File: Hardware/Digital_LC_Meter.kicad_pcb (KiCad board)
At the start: 2 copper layers, 139.7 x 139.7 mm, 0 parts

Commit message: updated kicad files
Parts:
- added C_BP1: 100nF, Capacitor_THT:C_Rect_L7.0mm_W2.0mm_P5.00mm, F.Cu at (127.0, 137.2)
- added C_COUP1: 10uF, Capacitor_THT:CP_Radial_D5.0mm_P2.50mm, F.Cu at (147.3, 120.7)
- added C_MICA1: 1nF, Capacitor_THT:C_Rect_L7.0mm_W2.0mm_P5.00mm, F.Cu at (152.4, 163.8)
- added C_MICA2: 1nF, Capacitor_THT:C_Rect_L7.0mm_W2.0mm_P5.00mm, F.Cu at (163.8, 158.8)
- added C_OSC1: 10uF, Capacitor_THT:CP_Radial_D5.0mm_P2.50mm, F.Cu at (102.9, 116.8)
- added J_CALJUMPER1: Conn_01x02, Connector_PinHeader_2.54mm:PinHeader_1x02_P2.54mm_Vertical, F.Cu at (83.8, 161.3)
- added J_DA1: Conn_01x01, Connector_PinHeader_2.54mm:PinHeader_1x01_P2.54mm_Vertical, F.Cu at (158.8, 83.8)
- added J_DK1: Conn_01x01, Connector_PinHeader_2.54mm:PinHeader_1x01_P2.54mm_Vertical, F.Cu at (166.4, 83.8)
- added J_ERASEBTN1: Conn_01x02, Connector_PinHeader_2.54mm:PinHeader_1x02_P2.54mm_Vertical, F.Cu at (73.7, 161.3)
- added J_INPUT1: Conn_01x02, Connector_PinHeader_2.54mm:PinHeader_1x02_P2.54mm_Vertical, F.Cu at (129.5, 97.8)
- added J_LCSELECTSPDT1: Conn_01x06, Connector_PinHeader_2.54mm:PinHeader_1x06_P2.54mm_Vertical, F.Cu at (138.4, 102.9)
- added J_NANOTX1: Conn_01x15, Connector_PinHeader_2.54mm:PinHeader_1x15_P2.54mm_Vertical, F.Cu at (52.1, 92.7)
- added J_NANOVIN1: Conn_01x15, Connector_PinHeader_2.54mm:PinHeader_1x15_P2.54mm_Vertical, F.Cu at (67.3, 92.7)
- added J_NUDGEBTN1: Conn_01x03, Connector_PinHeader_2.54mm:PinHeader_1x03_P2.54mm_Vertical, F.Cu at (92.7, 161.3)
- added J_OLED1: Conn_01x04, Connector_PinHeader_2.54mm:PinHeader_1x04_P2.54mm_Vertical, F.Cu at (118.1, 161.3)
- added J_PWR1: Conn_01x02, Connector_PinHeader_2.54mm:PinHeader_1x02_P2.54mm_Vertical, F.Cu at (153.7, 142.2)
- added J_RESETBTN1: Conn_01x02, Connector_PinHeader_2.54mm:PinHeader_1x02_P2.54mm_Vertical, F.Cu at (130.8, 161.3)
- added L1: 100uH, Inductor_THT:L_Radial_D7.8mm_P5.00mm_Fastron_07HCP, F.Cu at (147.3, 96.5)
- added R3: 100K, Resistor_THT:R_Axial_DIN0207_L6.3mm_D2.5mm_P7.62mm_Horizontal, F.Cu at (128.3, 115.6)
- added R_BIAS1: 100K, Resistor_THT:R_Axial_DIN0207_L6.3mm_D2.5mm_P7.62mm_Horizontal, F.Cu at (135.9, 113.0)
- added R_BIAS2: 100K, Resistor_THT:R_Axial_DIN0207_L6.3mm_D2.5mm_P7.62mm_Horizontal, F.Cu at (105.4, 108.0)
- added R_BIAS3: 4K7, Resistor_THT:R_Axial_DIN0207_L6.3mm_D2.5mm_P7.62mm_Horizontal, F.Cu at (119.4, 97.8)
- added R_OSC1: 47K, Resistor_THT:R_Axial_DIN0207_L6.3mm_D2.5mm_P7.62mm_Horizontal, F.Cu at (119.4, 127.0)
- added R_SIG1: 6K8, Resistor_THT:R_Axial_DIN0207_L6.3mm_D2.5mm_P7.62mm_Horizontal, F.Cu at (111.8, 91.4)
- added U_OSC1: LM311, Package_DIP:DIP-8_W7.62mm_Socket, F.Cu at (111.8, 113.0)
- added U_RLY1: TE_ReedRelay_V23100V4xxxA010, TE_Reed_Relay_V23100V4:TE_ReedRelay_V23100V4, F.Cu at (163.8, 101.6)
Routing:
- net /GND: track 0.00 -> 511.2 mm
- net /5V: track 0.00 -> 205.8 mm
- net /RELAY_PIN3: track 0.00 -> 171.1 mm
- net /VIN: track 0.00 -> 123.2 mm
- net /DECR_PIN4: track 0.00 -> 120.9 mm
- net /CL_BAR_PIN2: track 0.00 -> 117.9 mm
- net /IND_PARALLEL: track 0.11 -> 110.6 mm
- net /RESET_PIN: track 0.00 -> 107.0 mm
- net /OSC_SIG_PIN5: track 0.00 -> 100.7 mm
- net /SDA: track 0.00 -> 82.3 mm
- net /SCL: track 0.00 -> 81.5 mm
- net Net-(C_COUP1-Pad1): track 0.00 -> 75.5 mm
- net /CAL_ERASE_PIN8: track 0.00 -> 75.1 mm
- net /INCR_PIN6: track 0.00 -> 68.8 mm
- net /CAL_LK_PIN7: track 0.00 -> 60.4 mm
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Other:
- board size 139.7 x 139.7 mm -> 139.7 x 109.2 mm

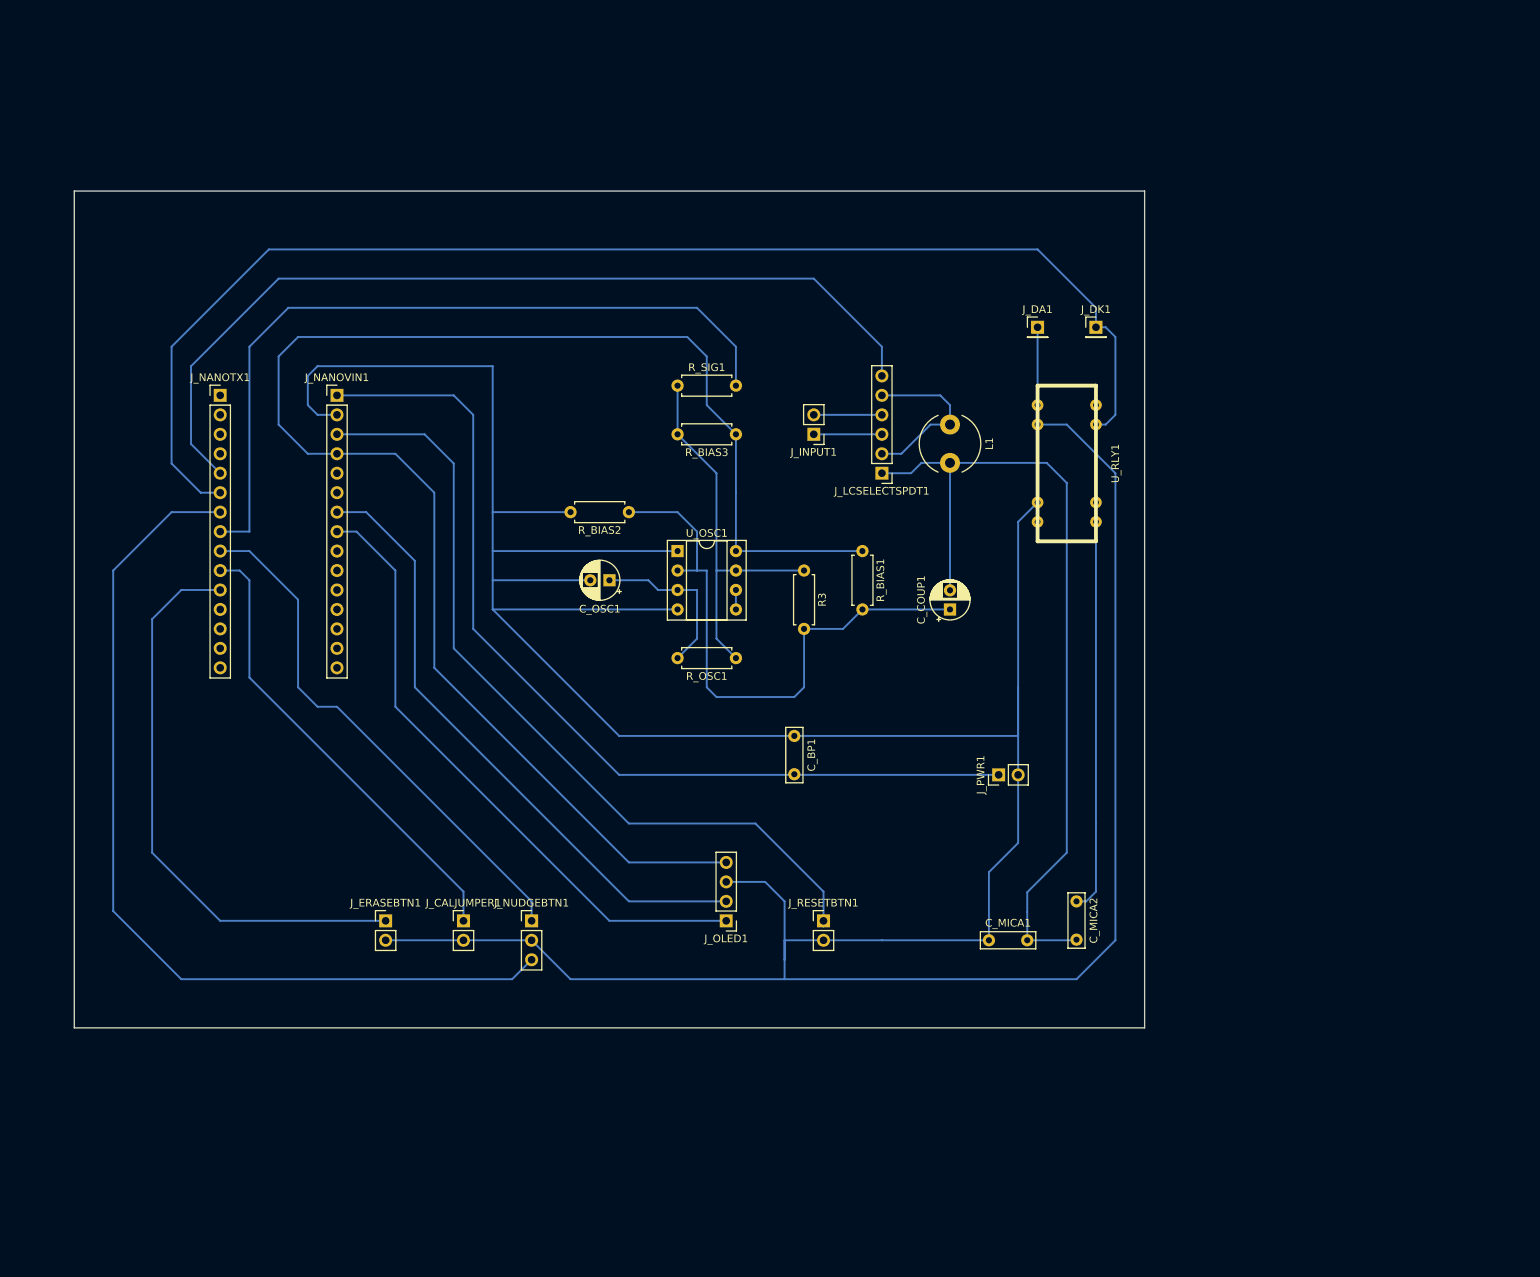
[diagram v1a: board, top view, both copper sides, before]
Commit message: Added 2nd OLED and TCA9548A IICMux. Updated Schematic and Board Layouts
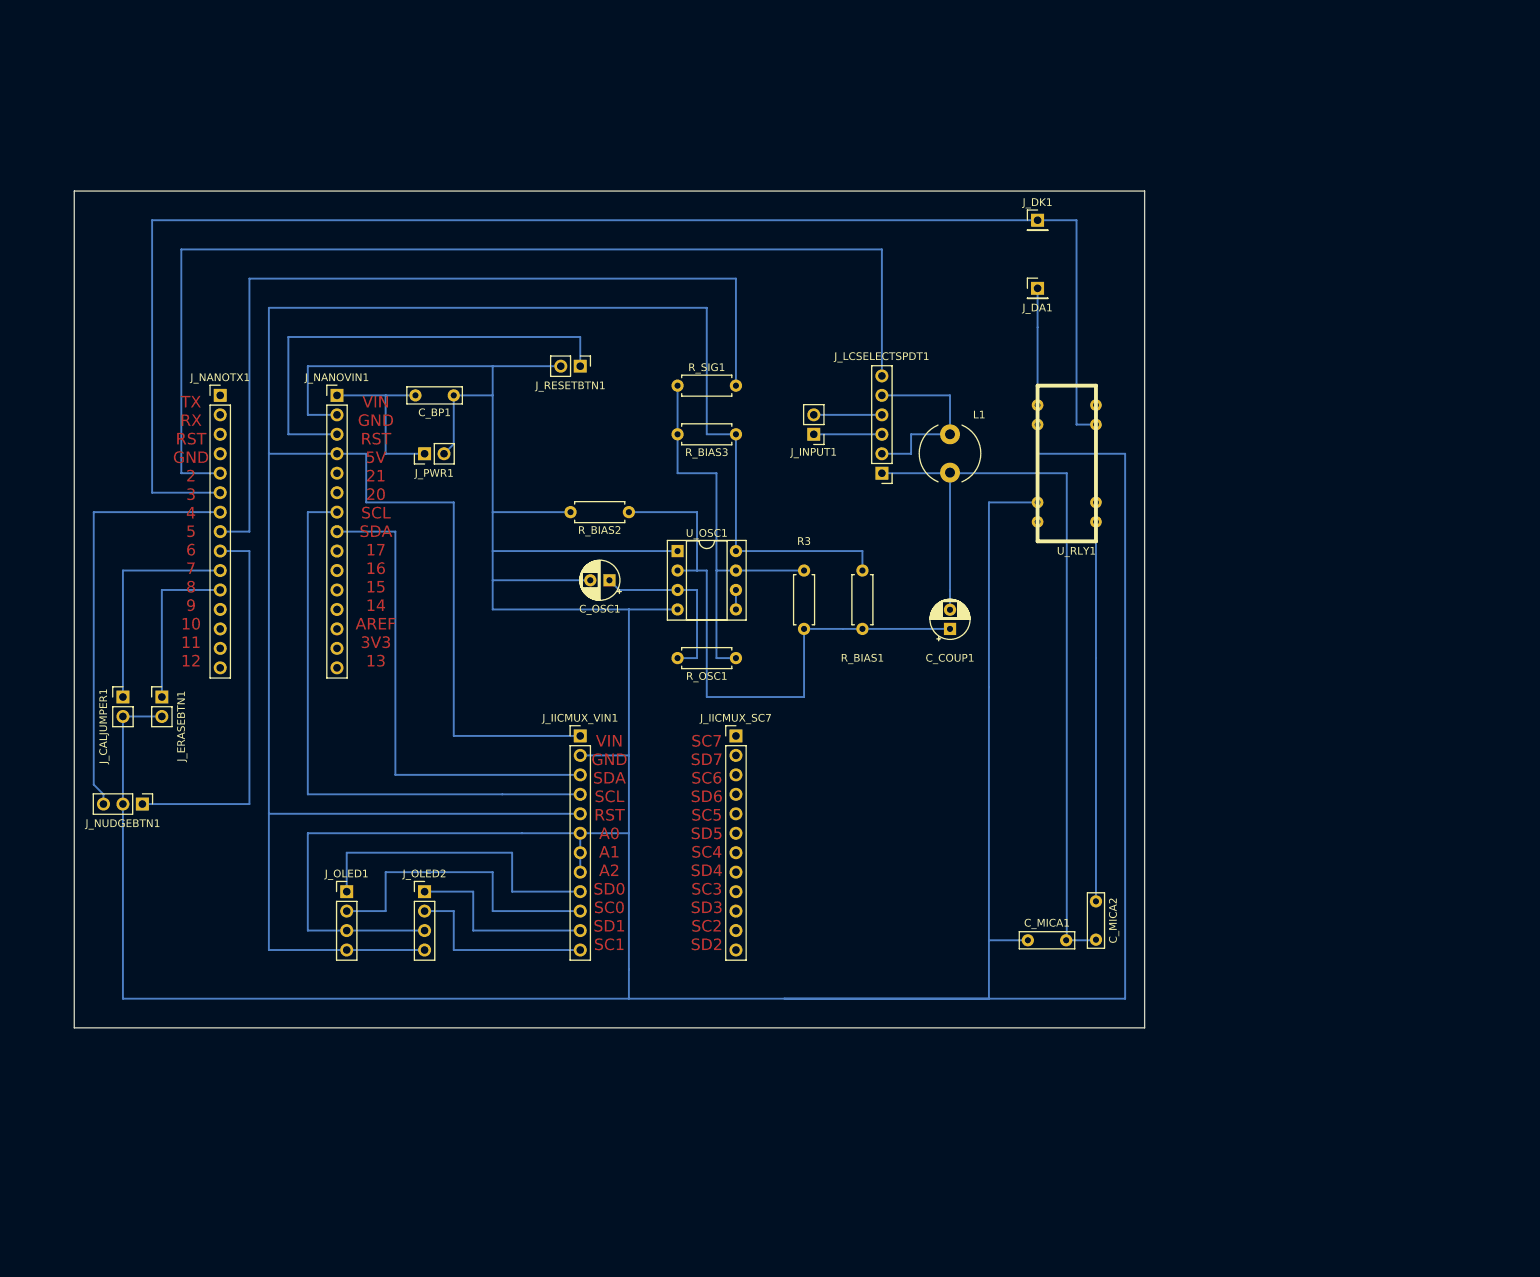
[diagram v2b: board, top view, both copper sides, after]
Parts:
- added J_IICMUX_SC7: Conn_01x12, Connector_PinHeader_2.54mm:PinHeader_1x12_P2.54mm_Vertical, F.Cu at (119.4, 137.2)
- added J_IICMUX_VIN1: Conn_01x12, Connector_PinHeader_2.54mm:PinHeader_1x12_P2.54mm_Vertical, F.Cu at (99.1, 137.2)
- added J_OLED2: Conn_01x04, Connector_PinHeader_2.54mm:PinHeader_1x04_P2.54mm_Vertical, F.Cu at (78.7, 157.5)
- moved J_PWR1 85.9 mm to (78.7, 100.3)
- moved J_RESETBTN1 79.0 mm to (99.1, 88.9), turned to 270 degrees
- moved C_BP1 62.9 mm to (82.5, 92.7), turned to 180 degrees
- moved J_CALJUMPER1 53.2 mm to (39.4, 132.1)
- moved J_NUDGEBTN1 53.0 mm to (41.9, 146.1), turned to 270 degrees
- moved J_OLED1 49.7 mm to (68.6, 157.5), turned to 0 degrees
- moved J_ERASEBTN1 41.3 mm to (44.5, 132.1)
- moved J_DK1 15.9 mm to (158.8, 69.8)
- moved J_DA1 5.08 mm to (158.8, 78.7)
- moved C_MICA1 5.08 mm to (157.5, 163.8)
- moved C_COUP1 2.54 mm to (147.3, 123.2)
- moved C_MICA2 2.54 mm to (166.4, 158.8)
- moved R_BIAS1 2.54 mm to (135.9, 115.6)
- moved L1 1.27 mm to (147.3, 97.8)
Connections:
- J_NANOTX1 pad 1: Net-(J_NANOTX1-Pad1) -> (no net)
- J_NANOTX1 pad 12: Net-(J_NANOTX1-Pad12) -> (no net)
- J_NANOTX1 pad 13: Net-(J_NANOTX1-Pad13) -> (no net)
- J_NANOTX1 pad 14: Net-(J_NANOTX1-Pad14) -> (no net)
- J_NANOTX1 pad 15: Net-(J_NANOTX1-Pad15) -> (no net)
- J_NANOTX1 pad 2: Net-(J_NANOTX1-Pad2) -> (no net)
- J_NANOTX1 pad 3: Net-(J_NANOTX1-Pad3) -> (no net)
- J_NANOTX1 pad 4: Net-(J_NANOTX1-Pad4) -> (no net)
- J_NANOVIN1 pad 10: Net-(J_NANOVIN1-Pad10) -> (no net)
- J_NANOVIN1 pad 11: Net-(J_NANOVIN1-Pad11) -> (no net)
- J_NANOVIN1 pad 12: Net-(J_NANOVIN1-Pad12) -> (no net)
- J_NANOVIN1 pad 13: Net-(J_NANOVIN1-Pad13) -> (no net)
- J_NANOVIN1 pad 14: Net-(J_NANOVIN1-Pad14) -> (no net)
- J_NANOVIN1 pad 15: Net-(J_NANOVIN1-Pad15) -> (no net)
- J_NANOVIN1 pad 5: Net-(J_NANOVIN1-Pad5) -> (no net)
- J_NANOVIN1 pad 6: Net-(J_NANOVIN1-Pad6) -> (no net)
- J_NANOVIN1 pad 9: Net-(J_NANOVIN1-Pad9) -> (no net)
- J_OLED1 pad 1: /SDA -> /SDA0
- J_OLED1 pad 2: /SCL -> /SCL0
- U_RLY1 pad 14: Net-(U_RLY1-Pad14) -> (no net)
- U_RLY1 pad 2: Net-(U_RLY1-Pad2) -> (no net)
- U_RLY1 pad 7: Net-(U_RLY1-Pad7) -> (no net)
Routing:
- net /GND: track 511.2 -> 671.1 mm
- net /5V: track 205.8 -> 334.0 mm
- net /VIN: track 123.2 -> 22.9 mm
- net /DECR_PIN4: track 120.9 -> 55.1 mm
- net /CAL_ERASE_PIN8: track 75.1 -> 21.6 mm
- net /RESET_PIN: track 107.0 -> 61.0 mm
- net /SCL0: track 0.00 -> 40.6 mm
- net /SDA0: track 0.00 -> 40.6 mm
- net /CAL_LK_PIN7: track 60.4 -> 29.2 mm
- net /SDA1: track 0.00 -> 25.4 mm
- net /SCL1: track 0.00 -> 25.4 mm
- net /CL_BAR_PIN2: track 117.9 -> 142.2 mm
- net /RELAY_PIN3: track 171.1 -> 194.3 mm
- net /SDA: track 82.3 -> 63.5 mm
- net /INCR_PIN6: track 68.8 -> 50.8 mm
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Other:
- board text added: "SC7 SD7 SC6 SD6 SC5 SD5 SC4 SD4 SC3 SD3 SC2 SD2"
- board text added: "TX RX RST GND 2 3 4 5 6 7 8 9 10 11 12"
- board text added: "VIN GND RST 5V 21 20 SCL SDA 17 16 15 14 AREF 3V3 13"
- board text added: "VIN GND SDA SCL RST A0 A1 A2 SD0 SC0 SD1 SC1"

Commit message: updates
- Added I2C Mux (TCA9548A) to design
- Initial prototype tested (firmware needs work)
- Created Front Panel Template for enclosure (Hammond 1455T1601)
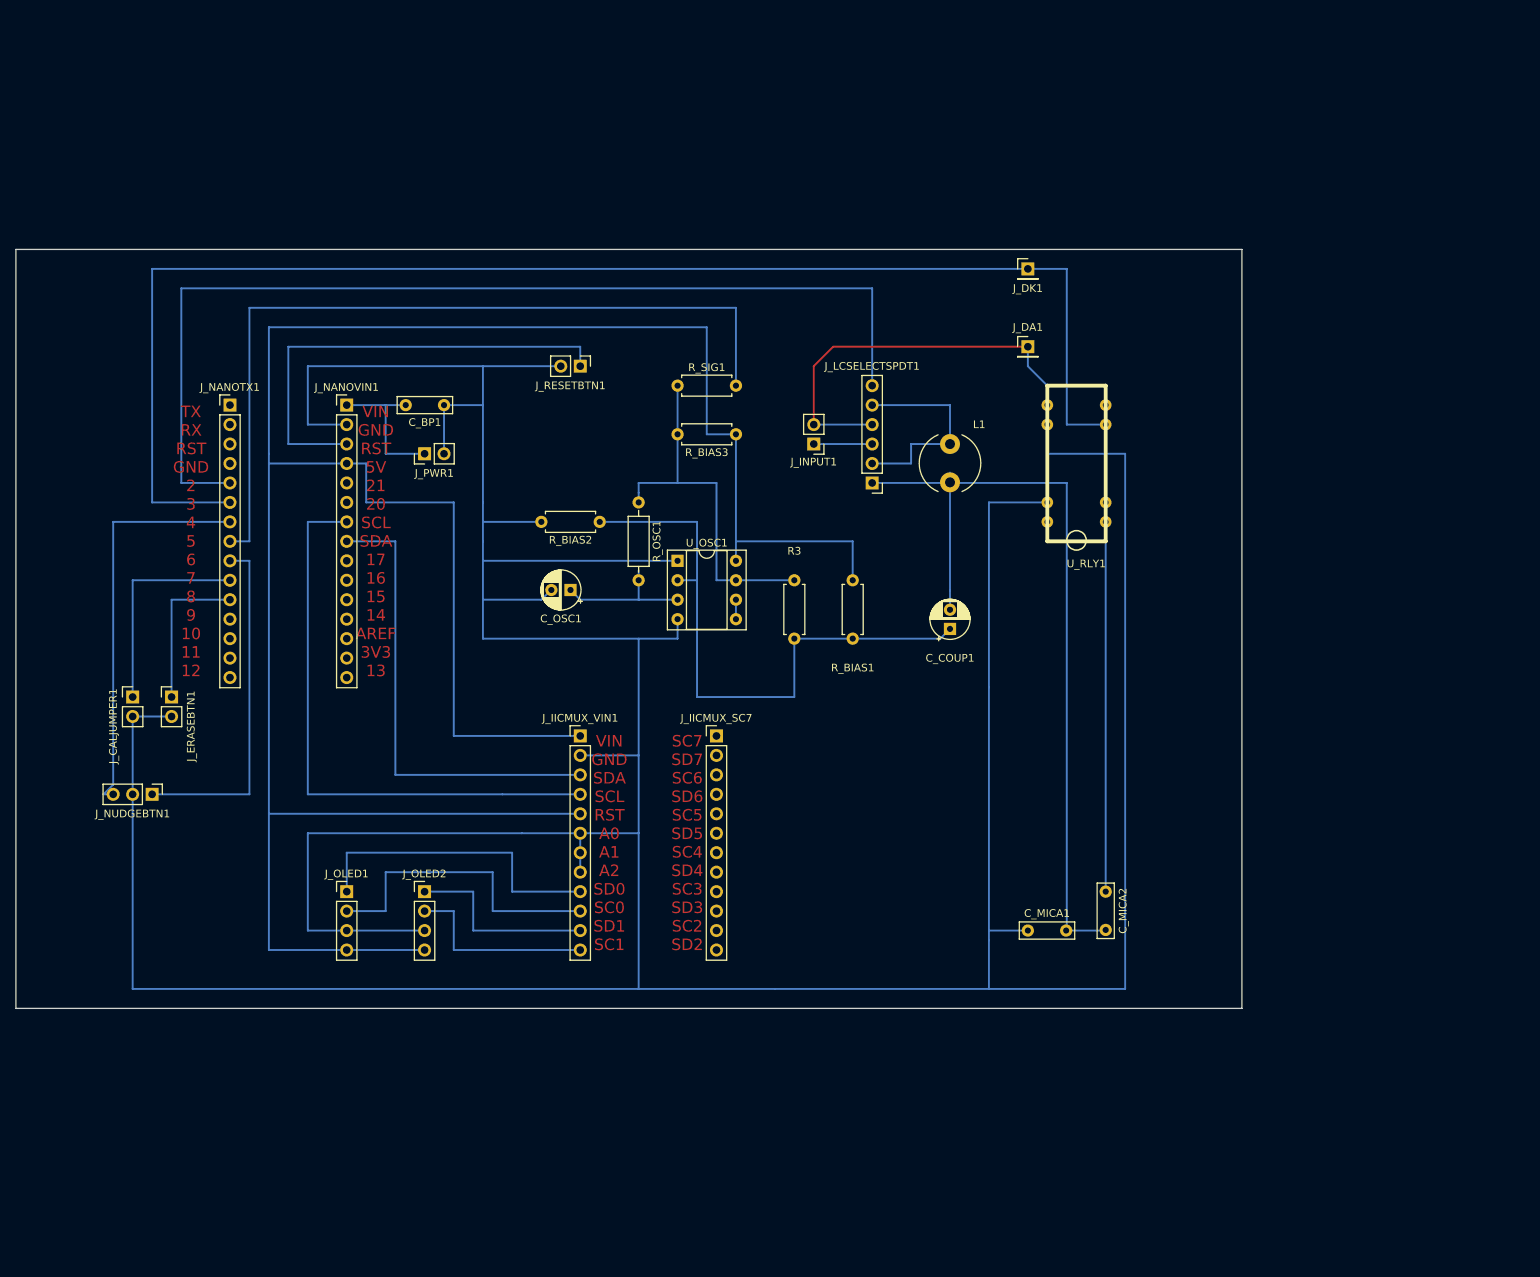
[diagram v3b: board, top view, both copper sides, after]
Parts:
- R_OSC1: footprint Resistor_THT:R_Axial_DIN0207_L6.3mm_D2.5mm_P7.62mm_Horizontal -> Resistor_THT:R_Axial_DIN0207_L6.3mm_D2.5mm_P10.16mm_Horizontal
- moved R_OSC1 24.0 mm to (106.7, 106.7), turned to 270 degrees
- moved J_DA1 7.73 mm to (157.5, 86.4)
- moved J_DK1 6.48 mm to (157.5, 76.2)
- moved C_OSC1 5.24 mm to (97.8, 118.1)
- moved R_BIAS2 4.02 mm to (101.6, 109.2)
- moved J_IICMUX_SC7 2.54 mm to (116.8, 137.2)
- moved R3 1.80 mm to (127.0, 116.8)
- moved J_NANOTX1 1.80 mm to (53.3, 94.0)
- moved J_NUDGEBTN1 1.80 mm to (43.2, 144.8)
- moved C_BP1 1.80 mm to (81.3, 94.0)
- moved J_LCSELECTSPDT1 1.80 mm to (137.2, 104.1)
- moved J_NANOVIN1 1.80 mm to (68.6, 94.0)
- moved C_MICA2 1.80 mm to (167.6, 157.5)
- moved R_BIAS1 1.80 mm to (134.6, 116.8)
- moved C_MICA1 1.27 mm to (157.5, 162.6)
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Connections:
- J_IICMUX_SC7 pad 1: (no net) -> Net-(J_IICMUX_SC7-Pad1)
- J_IICMUX_SC7 pad 10: (no net) -> Net-(J_IICMUX_SC7-Pad10)
- J_IICMUX_SC7 pad 11: (no net) -> Net-(J_IICMUX_SC7-Pad11)
- J_IICMUX_SC7 pad 12: (no net) -> Net-(J_IICMUX_SC7-Pad12)
- J_IICMUX_SC7 pad 2: (no net) -> Net-(J_IICMUX_SC7-Pad2)
- J_IICMUX_SC7 pad 3: (no net) -> Net-(J_IICMUX_SC7-Pad3)
- J_IICMUX_SC7 pad 4: (no net) -> Net-(J_IICMUX_SC7-Pad4)
- J_IICMUX_SC7 pad 5: (no net) -> Net-(J_IICMUX_SC7-Pad5)
- J_IICMUX_SC7 pad 6: (no net) -> Net-(J_IICMUX_SC7-Pad6)
- J_IICMUX_SC7 pad 7: (no net) -> Net-(J_IICMUX_SC7-Pad7)
- J_IICMUX_SC7 pad 8: (no net) -> Net-(J_IICMUX_SC7-Pad8)
- J_IICMUX_SC7 pad 9: (no net) -> Net-(J_IICMUX_SC7-Pad9)
- J_INPUT1 pad 2: Net-(J_INPUT1-Pad2) -> /GND
- J_LCSELECTSPDT1 pad 4: Net-(J_INPUT1-Pad2) -> /GND
- J_NANOTX1 pad 1: (no net) -> Net-(J_NANOTX1-Pad1)
- J_NANOTX1 pad 12: (no net) -> Net-(J_NANOTX1-Pad12)
- J_NANOTX1 pad 13: (no net) -> Net-(J_NANOTX1-Pad13)
- J_NANOTX1 pad 14: (no net) -> Net-(J_NANOTX1-Pad14)
- J_NANOTX1 pad 15: (no net) -> Net-(J_NANOTX1-Pad15)
- J_NANOTX1 pad 2: (no net) -> Net-(J_NANOTX1-Pad2)
- J_NANOTX1 pad 3: (no net) -> Net-(J_NANOTX1-Pad3)
- J_NANOTX1 pad 4: (no net) -> Net-(J_NANOTX1-Pad4)
- J_NANOVIN1 pad 10: (no net) -> Net-(J_NANOVIN1-Pad10)
- J_NANOVIN1 pad 11: (no net) -> Net-(J_NANOVIN1-Pad11)
- J_NANOVIN1 pad 12: (no net) -> Net-(J_NANOVIN1-Pad12)
- J_NANOVIN1 pad 13: (no net) -> Net-(J_NANOVIN1-Pad13)
- J_NANOVIN1 pad 14: (no net) -> Net-(J_NANOVIN1-Pad14)
- J_NANOVIN1 pad 15: (no net) -> Net-(J_NANOVIN1-Pad15)
- J_NANOVIN1 pad 5: (no net) -> Net-(J_NANOVIN1-Pad5)
- J_NANOVIN1 pad 6: (no net) -> Net-(J_NANOVIN1-Pad6)
- J_NANOVIN1 pad 9: (no net) -> Net-(J_NANOVIN1-Pad9)
- U_RLY1 pad 14: (no net) -> Net-(U_RLY1-Pad14)
- U_RLY1 pad 2: (no net) -> Net-(U_RLY1-Pad2)
- U_RLY1 pad 7: (no net) -> Net-(U_RLY1-Pad7)
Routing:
- net /RELAY_PIN3: track 194.3 -> 185.4 mm
- net Net-(J_INPUT1-Pad2): track 8.89 -> 0.00 mm
- net /CL_BAR_PIN2: track 142.2 -> 134.6 mm
- net /OSC_SIG_PIN5: track 114.3 -> 106.7 mm
- net /GND: track 671.1 -> 678.3 mm
- net Net-(R3-Pad1): track 54.6 -> 48.3 mm
- net /INCR_PIN6: track 50.8 -> 45.7 mm
- net Net-(C_OSC1-Pad1): track 23.4 -> 18.3 mm
- net /VIN: track 22.9 -> 19.0 mm
- net /5V: track 334.0 -> 330.2 mm
- net /SDA: track 63.5 -> 61.0 mm
- net /IND_SERIES: track 25.4 -> 27.9 mm
- net /DECR_PIN4: track 55.1 -> 52.6 mm
- net Net-(C_COUP1-Pad1): track 77.5 -> 79.3 mm
- net Net-(J_INPUT1-Pad1): track 8.89 -> 7.62 mm
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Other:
- board size 139.7 x 109.2 mm -> 160 x 99.1 mm
